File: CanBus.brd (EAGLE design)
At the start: 160 x 100 mm, 3 parts, among them IC1 MCP2515-I/P, IC2 MCP2551-E/P, X1 MAC64L

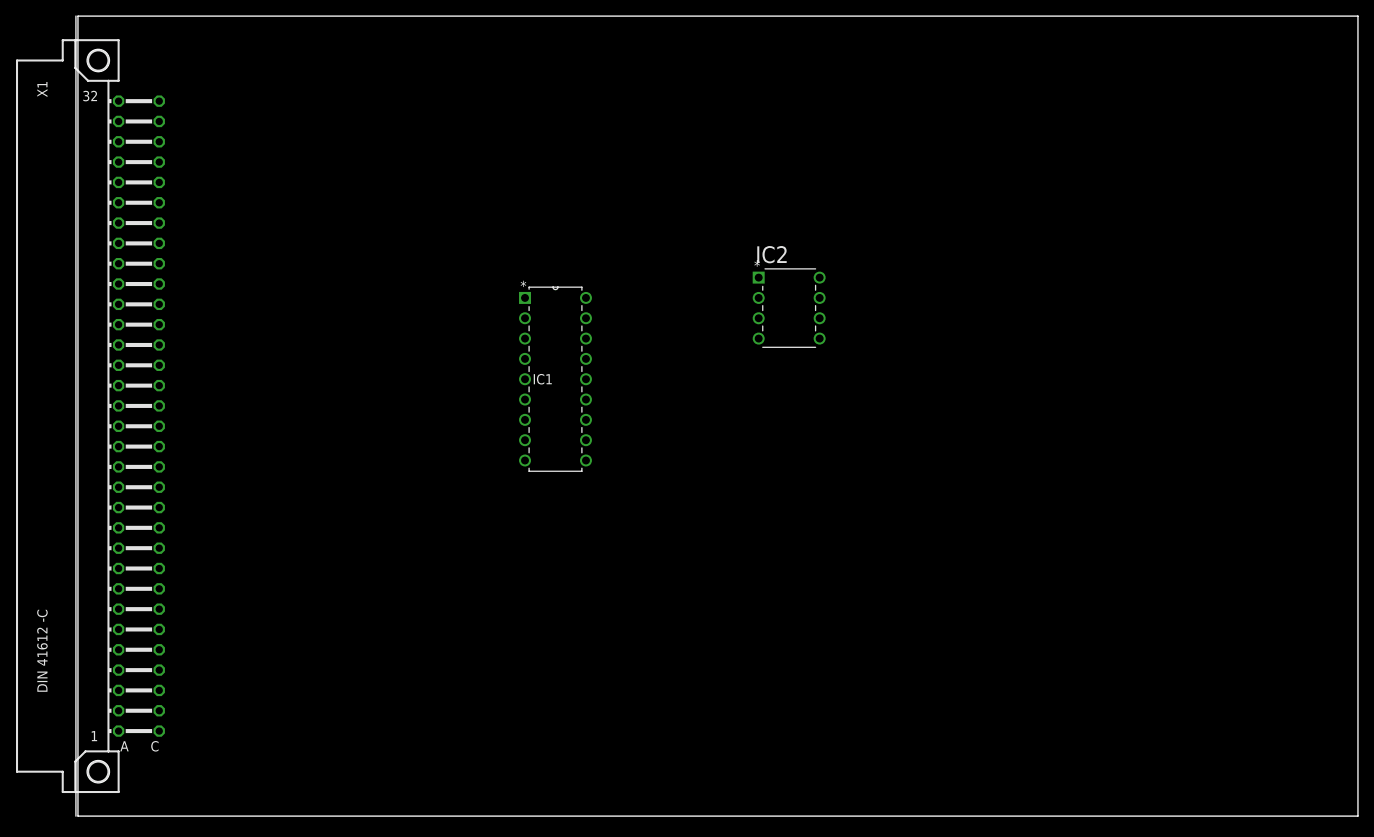
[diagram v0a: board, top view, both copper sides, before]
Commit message: Can-Bus, Reset für den RasPi, Kleinere Optimierungen
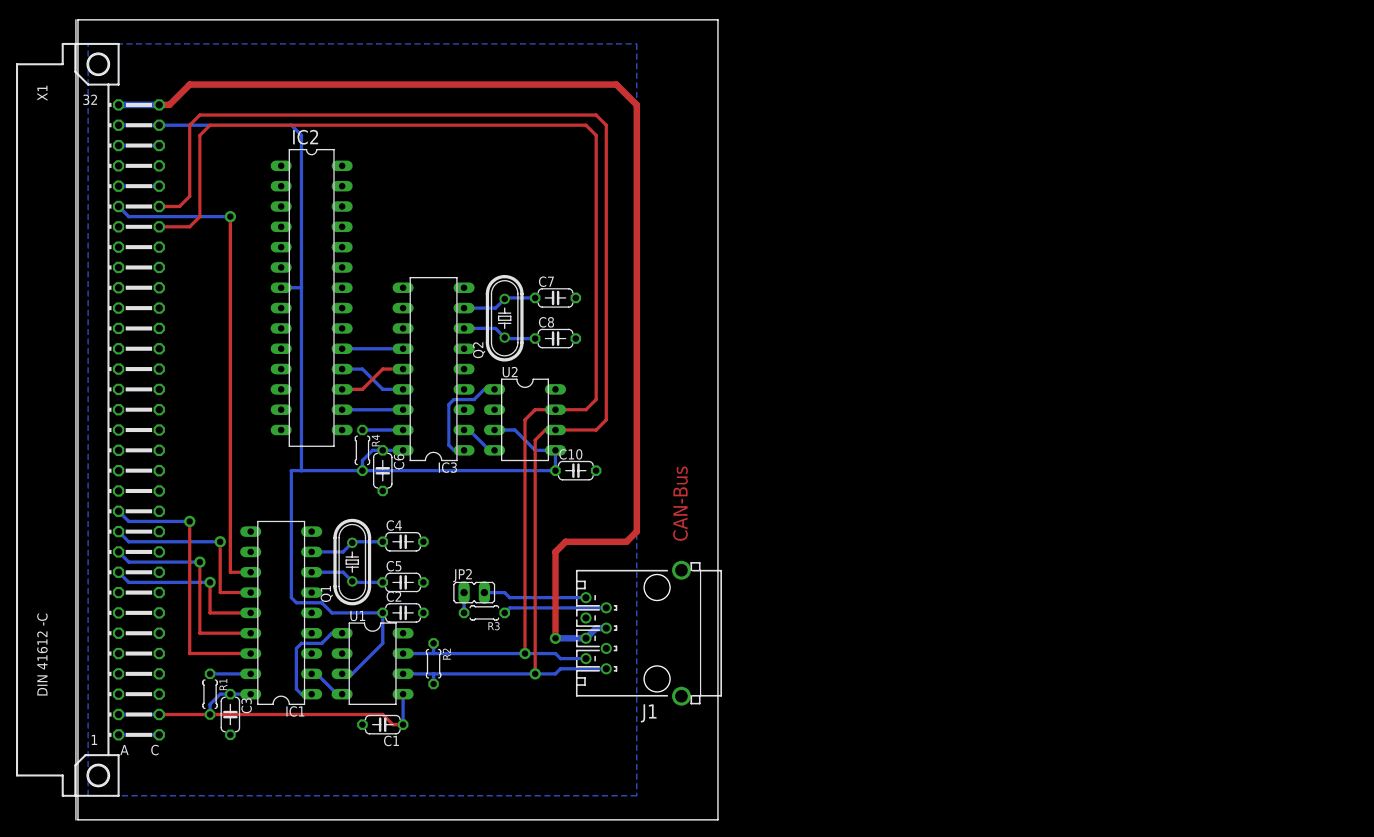
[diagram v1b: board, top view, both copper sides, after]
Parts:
- added C1, C10, C2, C3, C6: 100nF, rcl:C050-024X044
- added C4, C5, C7, C8: 22pF, rcl:C050-024X044
- added IC3: MCP2515-I/P, mcp2515_2551_2562:DIL18
- added J1: (no value), con-amp:555153-1
- added JP2: (no value), jumper:JP1
- added Q1, Q2: 16MHz, crystal:HC49/S
- added R1, R4: 4k7, rcl:0204/5
- added R2, R3: 120R, rcl:0204/5
- added U1, U2: MCP2562-E/P, mcp2515_2551_2562:DIL8
- IC1: device MCP2515:DIP254P762X432-18 -> mcp2515_2551_2562:DIL18
- IC2: value MCP2551-E/P -> MEGA8-P; device MCP2551:DIP254P762X432-8 -> atmel:DIL28-3
- moved IC2 63.7 mm to (29.2, 64.8), turned to 270 degrees
- moved IC1 42.6 mm to (25.4, 25.4), turned to 90 degrees
- moved X1 0.47 mm to (2.54, 49.5)
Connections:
- net PI_RESET renamed !PI_RESET
- removed net GND_INT: X1.A29, X1.A3, X1.A6, X1.A8, X1.C29, X1.C3, X1.C6, X1.C8
- removed net RS485_A: X1.C26
- removed net RS495_B: X1.C27
- removed net VDD: IC1.18, IC2.3
- removed net VSS: IC1.9
- new net AT_RXCAN: IC3.2, U2.4
- new net AT_SPI_CS: IC2.16, IC3.16
- new net AT_SPI_MISO: IC2.18, IC3.15
- new net AT_SPI_MOSI: IC2.17, IC3.14
- new net AT_SPI_SCK: IC2.19, IC3.13
- new net AT_TXCAN: IC3.1, U2.1
- new net AVCC: IC2.20
- new net CANH: J1.2, R2.1, U1.7, U2.7, X1.C26
- new net CANH_2: J1.7, R3.1
- new net CANL: J1.1, R2.2, U1.6, U2.6, X1.C27
- new net CANL_2: J1.8, JP2.2
- new net GND: C1.2, C10.2, C2.2, C3.2, C4.2, C5.2, C6.2, C7.2, C8.2, IC1.9, IC2.22, IC2.8, IC3.9, J1.3, J1.6, U1.2, U1.8, U2.2, U2.8, X1.A29, X1.A3, X1.A6, X1.A8, X1.C29, X1.C3, X1.C6, X1.C8
- new net N$1: C4.1, IC1.8, Q1.2
- new net N$2: IC1.17, R1.1
- new net N$3: JP2.1, R3.2
- new net N$4: C5.1, IC1.7, Q1.1
- new net N$5: IC3.17, R4.1
- new net N$6: C7.1, IC3.8, Q2.2
- new net N$7: C8.1, IC3.7, Q2.1
- new net RXCAN: IC1.2, U1.4
- new net TXCAN: IC1.1, U1.1
- net +24V: now also J1.4, J1.5
- net +3,3V: now also C1.1, C3.1, IC1.18, R1.2, U1.5
- net +5V_EXT: now also C10.1, C2.1, C6.1, IC2.7, IC3.18, R4.2, U1.3, U2.3, U2.5
- net GPIO.25: now also IC1.12
- net SPI_CE0: now also IC1.16
- net SPI_MISO: now also IC1.15
- net SPI_MOSI: now also IC1.14
- net SPI_SCLK: now also IC1.13
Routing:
- net CANL: track 0.00 -> 169.3 mm, vias 0 -> 1
- net CANH: track 0.00 -> 162.9 mm, vias 0 -> 1
- net +5V_EXT: track 0.00 -> 157.5 mm
- net +24V: track 0.00 -> 149.1 mm, vias 0 -> 1
- net GPIO.25: track 0.00 -> 61.5 mm, vias 0 -> 1
- net +3,3V: track 0.00 -> 46.8 mm
- net SPI_CE0: track 0.00 -> 33.5 mm, vias 0 -> 1
- net SPI_MISO: track 0.00 -> 25.9 mm, vias 0 -> 1
- net SPI_SCLK: track 0.00 -> 23.4 mm, vias 0 -> 1
- net SPI_MOSI: track 0.00 -> 20.8 mm, vias 0 -> 1
- net AT_TXCAN: track 0.00 -> 13.8 mm
- net TXCAN: track 0.00 -> 13.8 mm
- net CANL_2: track 0.00 -> 13.0 mm
- net CANH_2: track 0.00 -> 13.0 mm
- net N$7: track 0.00 -> 9.42 mm
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- added copper zone on layer 16, net GND
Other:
- board size 160 x 100 mm -> 80 x 100 mm
- board text added: "CAN-Bus"

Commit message: Diverse Anpassungen
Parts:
- IC1, IC3: value MCP2515-I/P -> MCP2515-I/SO; device mcp2515_2551_2562:DIL18 -> mcp2515_2551_2562:SO18L
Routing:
- net AT_TXCAN: track 13.8 -> 18.1 mm
- net TXCAN: track 13.8 -> 18.1 mm
- net RXCAN: track 4.86 -> 8.06 mm
- net AT_RXCAN: track 4.86 -> 8.06 mm
- net +5V_EXT: track 157.5 -> 160.2 mm
- net +3,3V: track 46.8 -> 49.5 mm
- net SPI_MOSI: track 20.8 -> 19.8 mm
- net AT_SPI_MOSI: track 8.67 -> 7.58 mm
- net AT_SPI_SCK: track 7.62 -> 6.65 mm
- net SPI_MISO: track 25.9 -> 25.0 mm
- net N$1: track 9.42 -> 10.2 mm
- net N$6: track 9.42 -> 10.2 mm
- net SPI_SCLK: track 23.4 -> 22.6 mm
- net SPI_CE0: track 33.5 -> 32.9 mm
- net AT_SPI_CS: track 7.62 -> 7.00 mm
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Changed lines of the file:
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@@
 <elements>
 <element name="X1" library="con-vg" package="MAC64L" value="MAC64L" x="2.54" y="49.53" rot="R180"/>
-<element name="IC1" library="mcp2515_2551_2562" package="DIL18" value="MCP2515-I/P" x="25.4" y="25.4" rot="R90"/>
+<element name="IC1" library="mcp2515_2551_2562" package="SO18L" value="MCP2515-I/SO" x="25.4" y="25.4" rot="R90"/>
 <element name="J1" library="con-amp" package="555153-1" value="" x="72.39" y="22.86" rot="R90"/>
 <element name="U1" library="mcp2515_2551_2562" package="DIL8" value="MCP2562-E/P" x="31.75" y="20.32" rot="R270"/>
@@
 <attribute name="OC_NEWARK" value="unknown" x="29.21" y="64.77" size="1.778" layer="27" rot="R270" display="off"/>
 </element>
-<element name="IC3" library="mcp2515_2551_2562" package="DIL18" value="MCP2515-I/P" x="44.45" y="55.88" rot="R90"/>
+<element name="IC3" library="mcp2515_2551_2562" package="SO18L" value="MCP2515-I/SO" x="44.45" y="55.88" rot="R90"/>
 <element name="C6" library="rcl" package="C050-024X044" value="100nF" x="38.1" y="43.18" rot="R270"/>
 <element name="R4" library="rcl" package="0204/5" value="4k7" x="35.56" y="45.72" rot="R270"/>
@@
 <via x="16.51" y="29.21" extent="1-16" drill="0.8" diameter="1.4224"/>
 <wire x1="16.51" y1="29.21" x2="16.51" y2="25.4" width="0.4064" layer="1"/>
-<wire x1="16.51" y1="25.4" x2="21.59" y2="25.4" width="0.4064" layer="1"/>
+<wire x1="16.51" y1="25.4" x2="20.4978" y2="25.4" width="0.4064" layer="1"/>
 </signal>
 <signal name="SPI_MISO">
@@
 <via x="15.24" y="31.75" extent="1-16" drill="0.8" diameter="1.4224"/>
 <wire x1="15.24" y1="31.75" x2="15.24" y2="22.86" width="0.4064" layer="1"/>
-<wire x1="15.24" y1="22.86" x2="21.59" y2="22.86" width="0.4064" layer="1"/>
+<wire x1="15.24" y1="22.86" x2="20.4978" y2="24.13" width="0.4064" layer="1"/>
 </signal>
 <signal name="SPI_SCLK">
@@
 <via x="17.78" y="34.29" extent="1-16" drill="0.8" diameter="1.4224"/>
 <wire x1="17.78" y1="34.29" x2="17.78" y2="27.94" width="0.4064" layer="1"/>
-<wire x1="17.78" y1="27.94" x2="21.59" y2="27.94" width="0.4064" layer="1"/>
+<wire x1="17.78" y1="27.94" x2="20.4978" y2="26.67" width="0.4064" layer="1"/>
 </signal>
 <signal name="SPI_CE0">
@@
 <via x="13.97" y="36.83" extent="1-16" drill="0.8" diameter="1.4224"/>
 <wire x1="13.97" y1="36.83" x2="13.97" y2="20.32" width="0.4064" layer="1"/>
-<wire x1="13.97" y1="20.32" x2="21.59" y2="20.32" width="0.4064" layer="1"/>
+<wire x1="13.97" y1="20.32" x2="20.4978" y2="22.86" width="0.4064" layer="1"/>
 </signal>
 <signal name="SPI_CE1">
@@
 <via x="19.05" y="74.93" extent="1-16" drill="0.8" diameter="1.4224"/>
 <wire x1="19.05" y1="74.93" x2="19.05" y2="30.48" width="0.4064" layer="1"/>
-<wire x1="19.05" y1="30.48" x2="21.59" y2="30.48" width="0.4064" layer="1"/>
+<wire x1="19.05" y1="30.48" x2="20.4978" y2="27.94" width="0.4064" layer="1"/>
 </signal>
 <signal name="+3,3V">
@@
 <contactref element="C3" pad="1"/>
 <contactref element="R1" pad="2"/>
-<wire x1="21.59" y1="15.24" x2="19.05" y2="15.24" width="0.4064" layer="16"/>
+<wire x1="20.4978" y1="20.32" x2="19.05" y2="15.24" width="0.4064" layer="16"/>
 <wire x1="19.05" y1="15.24" x2="17.78" y2="15.24" width="0.4064" layer="16"/>
 <wire x1="17.78" y1="15.24" x2="16.51" y2="13.97" width="0.4064" layer="16"/>
@@
 <contactref element="C6" pad="1"/>
 <contactref element="R4" pad="2"/>
-<wire x1="40.64" y1="45.72" x2="38.1" y2="45.72" width="0.4064" layer="16"/>
+<wire x1="39.5478" y1="50.8" x2="38.1" y2="45.72" width="0.4064" layer="16"/>
 <wire x1="38.1" y1="45.72" x2="36.83" y2="45.72" width="0.4064" layer="16"/>
 <wire x1="36.83" y1="45.72" x2="35.56" y2="44.45" width="0.4064" layer="16"/>
@@
 <contactref element="IC1" pad="1"/>
 <contactref element="U1" pad="1"/>
-<wire x1="29.21" y1="15.24" x2="27.94" y2="15.24" width="0.4064" layer="16"/>
+<wire x1="30.3022" y1="20.32" x2="27.94" y2="15.24" width="0.4064" layer="16"/>
 <wire x1="27.94" y1="15.24" x2="27.305" y2="15.875" width="0.4064" layer="16"/>
 <wire x1="27.305" y1="15.875" x2="27.305" y2="20.955" width="0.4064" layer="16"/>
@@
 <wire x1="33.02" y1="15.24" x2="32.385" y2="15.24" width="0.4064" layer="16"/>
 <wire x1="32.385" y1="15.24" x2="29.845" y2="17.78" width="0.4064" layer="16"/>
-<wire x1="29.845" y1="17.78" x2="29.21" y2="17.78" width="0.4064" layer="16"/>
+<wire x1="29.845" y1="17.78" x2="30.3022" y2="21.59" width="0.4064" layer="16"/>
 </signal>
 <signal name="CANL">
@@
 <contactref element="IC1" pad="17"/>
 <contactref element="R1" pad="1"/>
-<wire x1="21.59" y1="17.78" x2="16.51" y2="17.78" width="0.4064" layer="16"/>
+<wire x1="20.4978" y1="21.59" x2="16.51" y2="17.78" width="0.4064" layer="16"/>
 </signal>
 <signal name="CANL_2">
@@
 <contactref element="Q1" pad="2"/>
 <contactref element="C4" pad="1"/>
-<wire x1="29.21" y1="33.02" x2="33.147" y2="33.02" width="0.4064" layer="16"/>
+<wire x1="30.3022" y1="29.21" x2="33.147" y2="33.02" width="0.4064" layer="16"/>
 <wire x1="33.147" y1="33.02" x2="34.29" y2="34.163" width="0.4064" layer="16"/>
 <wire x1="38.1" y1="34.29" x2="34.417" y2="34.29" width="0.4064" layer="16"/>
@@
 <contactref element="IC1" pad="7"/>
 <contactref element="C5" pad="1"/>
-<wire x1="29.21" y1="30.48" x2="33.147" y2="30.48" width="0.4064" layer="16"/>
+<wire x1="30.3022" y1="27.94" x2="33.147" y2="30.48" width="0.4064" layer="16"/>
 <wire x1="33.147" y1="30.48" x2="34.29" y2="29.337" width="0.4064" layer="16"/>
 <wire x1="38.1" y1="29.21" x2="34.417" y2="29.21" width="0.4064" layer="16"/>
@@
 <contactref element="IC3" pad="17"/>
 <contactref element="R4" pad="1"/>
-<wire x1="40.64" y1="48.26" x2="35.56" y2="48.26" width="0.4064" layer="16"/>
+<wire x1="39.5478" y1="52.07" x2="35.56" y2="48.26" width="0.4064" layer="16"/>
 </signal>
 <signal name="N$6">
@@
 <contactref element="Q2" pad="2"/>
 <contactref element="C7" pad="1"/>
-<wire x1="48.26" y1="63.5" x2="52.197" y2="63.5" width="0.4064" layer="16"/>
+<wire x1="49.3522" y1="59.69" x2="52.197" y2="63.5" width="0.4064" layer="16"/>
 <wire x1="52.197" y1="63.5" x2="53.34" y2="64.643" width="0.4064" layer="16"/>
 <wire x1="57.15" y1="64.77" x2="53.467" y2="64.77" width="0.4064" layer="16"/>
@@
 <contactref element="IC3" pad="7"/>
 <contactref element="C8" pad="1"/>
-<wire x1="48.26" y1="60.96" x2="52.197" y2="60.96" width="0.4064" layer="16"/>
+<wire x1="49.3522" y1="58.42" x2="52.197" y2="60.96" width="0.4064" layer="16"/>
 <wire x1="52.197" y1="60.96" x2="53.34" y2="59.817" width="0.4064" layer="16"/>
 <wire x1="57.15" y1="59.69" x2="53.467" y2="59.69" width="0.4064" layer="16"/>
@@
 <wire x1="33.02" y1="55.88" x2="35.56" y2="55.88" width="0.4064" layer="16"/>
 <wire x1="35.56" y1="55.88" x2="38.1" y2="53.34" width="0.4064" layer="16"/>
-<wire x1="38.1" y1="53.34" x2="40.64" y2="53.34" width="0.4064" layer="16"/>
+<wire x1="38.1" y1="53.34" x2="39.5478" y2="54.61" width="0.4064" layer="16"/>
 </signal>
 <signal name="AT_SPI_SCK">
 <contactref element="IC2" pad="19"/>
 <contactref element="IC3" pad="13"/>
-<wire x1="33.02" y1="58.42" x2="40.64" y2="58.42" width="0.4064" layer="16"/>
+<wire x1="33.02" y1="58.42" x2="39.5478" y2="57.15" width="0.4064" layer="16"/>
 </signal>
 <signal name="AT_SPI_MOSI">
@@
 <wire x1="33.02" y1="53.34" x2="35.56" y2="53.34" width="0.4064" layer="1"/>
 <wire x1="35.56" y1="53.34" x2="38.1" y2="55.88" width="0.4064" layer="1"/>
-<wire x1="38.1" y1="55.88" x2="40.64" y2="55.88" width="0.4064" layer="1"/>
+<wire x1="38.1" y1="55.88" x2="39.5478" y2="55.88" width="0.4064" layer="1"/>
 </signal>
 <signal name="AT_SPI_CS">
 <contactref element="IC2" pad="16"/>
 <contactref element="IC3" pad="16"/>
-<wire x1="33.02" y1="50.8" x2="40.64" y2="50.8" width="0.4064" layer="16"/>
+<wire x1="33.02" y1="50.8" x2="39.5478" y2="53.34" width="0.4064" layer="16"/>
 </signal>
 <signal name="AT_TXCAN">
 <contactref element="IC3" pad="1"/>
 <contactref element="U2" pad="1"/>
-<wire x1="48.26" y1="45.72" x2="46.99" y2="45.72" width="0.4064" layer="16"/>
+<wire x1="49.3522" y1="50.8" x2="46.99" y2="45.72" width="0.4064" layer="16"/>
 <wire x1="46.99" y1="45.72" x2="46.355" y2="46.355" width="0.4064" layer="16"/>
 <wire x1="46.355" y1="46.355" x2="46.355" y2="51.435" width="0.4064" layer="16"/>
@@
 <contactref element="IC3" pad="2"/>
 <contactref element="U2" pad="4"/>
-<wire x1="48.26" y1="48.26" x2="48.895" y2="48.26" width="0.4064" layer="16"/>
+<wire x1="49.3522" y1="52.07" x2="48.895" y2="48.26" width="0.4064" layer="16"/>
 <wire x1="48.895" y1="48.26" x2="51.435" y2="45.72" width="0.4064" layer="16"/>
 <wire x1="51.435" y1="45.72" x2="52.07" y2="45.72" width="0.4064" layer="16"/>
